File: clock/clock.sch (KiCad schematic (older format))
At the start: 166 parts, among them J1 Conn_02x05_Odd_Even, P1 Conn_WallPlug, T1 120 to 5, U1 74HC596, U10 74HC596, U11 LPC804-TSSOP24, U2 74HC596, U3 74HC596, U4 74HC596, U5 74HC596, U6 74HC596, U7 AP2204R-3.3, U8 74HC596, U9 74HC596

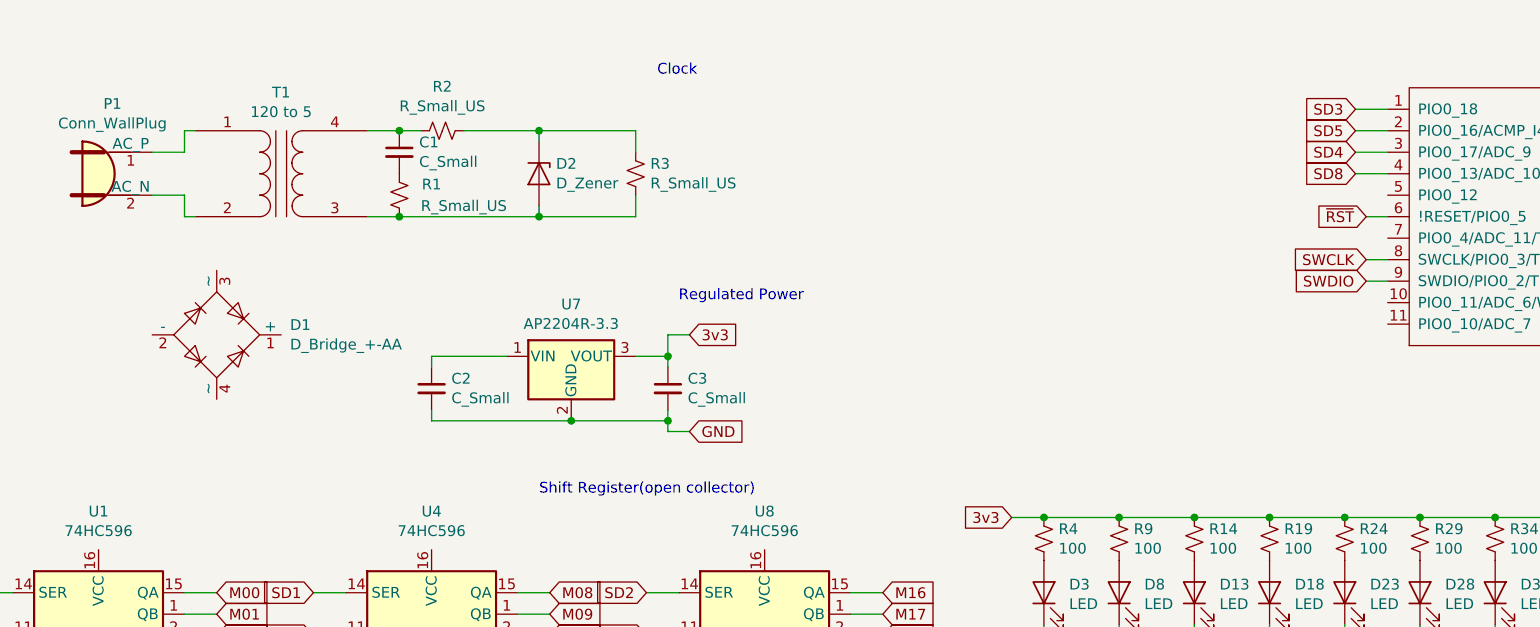
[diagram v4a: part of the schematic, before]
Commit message: Decided on a full wave rectifier. Reevaluated the desired transformer and chose a 120 to 12. Reevaluation due to minimum vin on 3v3 rec is 5v3. Added simulations images from QUCS to the build. QUCS used to design the clock timer edge. I might want to have some means for it to sync milliseconds externally, but that might be the feature creep that kills the project. If there are pins left over, pull them aside as an expansion header.
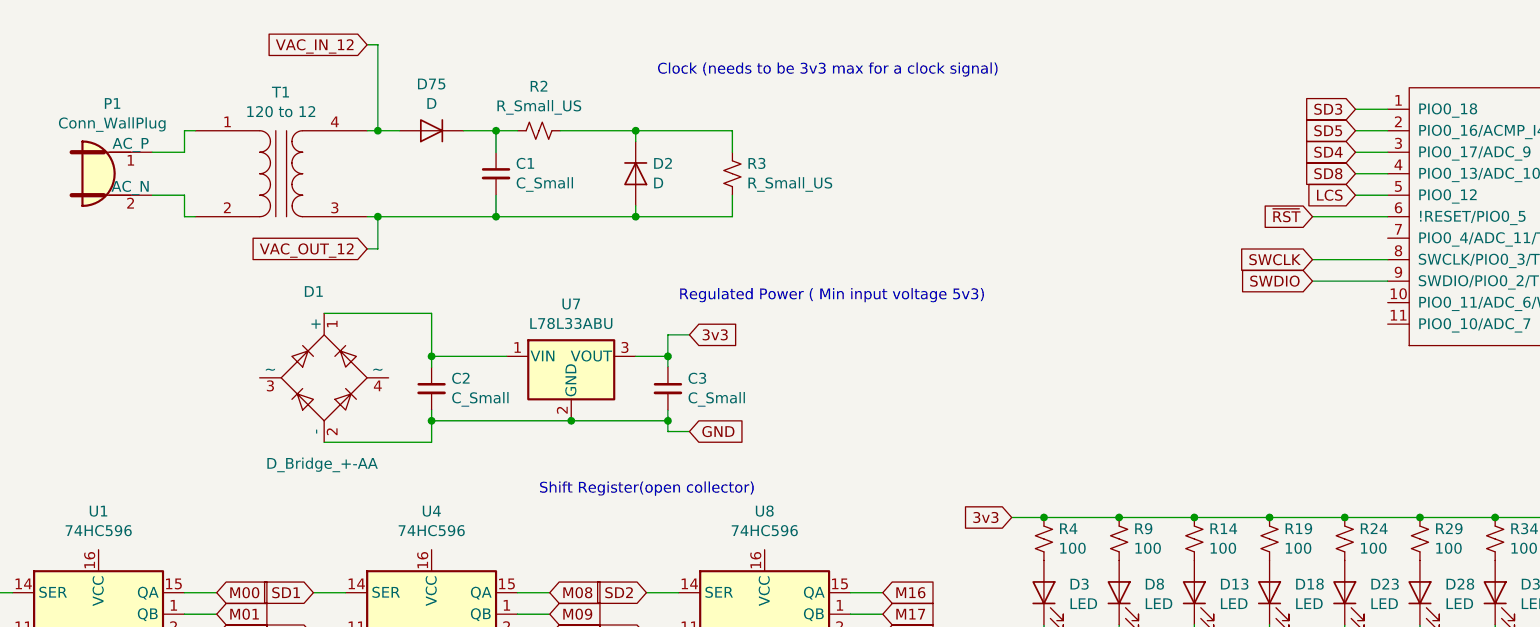
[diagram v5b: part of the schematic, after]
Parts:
- removed D2: D_Zener, symbol Device:D_Zener
- removed R1: R_Small_US, symbol Device:R_Small_US
- added D2, D75: D, symbol Device:D
- T1: value 120 to 5 -> 120 to 12
- U7: value AP2204R-3.3 -> L78L33ABU
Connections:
- net GND: now also D1.2 (-)
- net VAC_OUT_12: now reaches R3.1, T1.3 (SA)
- net VAC_OUT_12: now also C1.2, D2.2 (A)
- net at C1.1, R2.2: now also D75.1 (K); no longer T1.4 (SB)
- net at R2.1, R3.2: now also D2.1 (K)
- net at D1.1 (+): now also C2.1, U7.1 (VIN)
- net LCS: now reaches U11.5 (PIO0_12)
- new net VAC_IN_12: D75.2 (A), T1.4 (SB)
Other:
- note added: "Clock (needs to be 3v3 max for a clock signal)"
- note added: "Regulated Power ( Min input voltage 5v3)"
- note removed: "Clock"
- note removed: "Regulated Power"
- moved on the sheet: C1, D1, R2, R3
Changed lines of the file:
@@
 P 2100 1250
 F 0 "T1" H 2100 1628 50  0000 C CNN
-F 1 "120 to 5" H 2100 1537 50  0000 C CNN
+F 1 "120 to 12" H 2100 1537 50  0000 C CNN
 F 2 "" H 2100 1250 50  0001 C CNN
 F 3 "~" H 2100 1250 50  0001 C CNN
@@
 $EndComp
 $Comp
-L Device:D_Zener D2
-U 1 1 5DF1C116
-P 3300 1250
-F 0 "D2" V 3254 1329 50  0000 L CNN
-F 1 "D_Zener" V 3345 1329 50  0000 L CNN
-F 2 "" H 3300 1250 50  0001 C CNN
-F 3 "~" H 3300 1250 50  0001 C CNN
-	1    3300 1250
-	0    1    1    0
-$EndComp
-$Comp
 L Device:R_Small_US R2
 U 1 1 5DF1C1DC
-P 2850 1050
-F 0 "R2" V 2645 1050 50  0000 C CNN
-F 1 "R_Small_US" V 2736 1050 50  0000 C CNN
-F 2 "" H 2850 1050 50  0001 C CNN
-F 3 "~" H 2850 1050 50  0001 C CNN
-	1    2850 1050
+P 3300 1050
+F 0 "R2" V 3095 1050 50  0000 C CNN
+F 1 "R_Small_US" V 3186 1050 50  0000 C CNN
+F 2 "" H 3300 1050 50  0001 C CNN
+F 3 "~" H 3300 1050 50  0001 C CNN
+	1    3300 1050
 	0    1    1    0
 $EndComp
@@
 L Device:R_Small_US R3
 U 1 1 5DF1C2BA
-P 3750 1250
-F 0 "R3" H 3682 1204 50  0000 R CNN
-F 1 "R_Small_US" H 3682 1295 50  0000 R CNN
-F 2 "" H 3750 1250 50  0001 C CNN
-F 3 "~" H 3750 1250 50  0001 C CNN
-	1    3750 1250
+P 4200 1250
+F 0 "R3" H 4132 1204 50  0000 R CNN
+F 1 "R_Small_US" H 4132 1295 50  0000 R CNN
+F 2 "" H 4200 1250 50  0001 C CNN
+F 3 "~" H 4200 1250 50  0001 C CNN
+	1    4200 1250
 	-1   0    0    1
 $EndComp
@@
 L Device:C_Small C1
 U 1 1 5DF1C4C1
-P 2650 1150
-F 0 "C1" H 2742 1196 50  0000 L CNN
-F 1 "C_Small" H 2742 1105 50  0000 L CNN
-F 2 "" H 2650 1150 50  0001 C CNN
-F 3 "~" H 2650 1150 50  0001 C CNN
-	1    2650 1150
+P 3100 1250
+F 0 "C1" H 3192 1296 50  0000 L CNN
+F 1 "C_Small" H 3192 1205 50  0000 L CNN
+F 2 "" H 3100 1250 50  0001 C CNN
+F 3 "~" H 3100 1250 50  0001 C CNN
+	1    3100 1250
 	1    0    0    -1
 $EndComp
-$Comp
-L Device:R_Small_US R1
-U 1 1 5DF1C5AB
-P 2650 1350
-F 0 "R1" H 2500 1300 50  0000 C CNN
-F 1 "R_Small_US" H 2350 1400 50  0000 C CNN
-F 2 "" H 2650 1350 50  0001 C CNN
-F 3 "~" H 2650 1350 50  0001 C CNN
-	1    2650 1350
-	-1   0    0    1
-$EndComp
 Wire Wire Line
-	2500 1050 2650 1050
+	2950 1050 3100 1050
 Wire Wire Line
-	2650 1050 2750 1050
-Connection ~ 2650 1050
+	3100 1050 3200 1050
 Wire Wire Line
-	2950 1050 3300 1050
+	3400 1050 3750 1050
 Wire Wire Line
-	3300 1050 3300 1100
+	3750 1050 3750 1100
 Wire Wire Line
-	3300 1050 3750 1050
+	3750 1050 4200 1050
 Wire Wire Line
-	3750 1050 3750 1150
-Connection ~ 3300 1050
+	4200 1050 4200 1150
+Connection ~ 3750 1050
 Wire Wire Line
-	2500 1450 2650 1450
+	3750 1450 3750 1400
 Wire Wire Line
-	2650 1450 3300 1450
+	3750 1450 4200 1450
 Wire Wire Line
-	3300 1450 3300 1400
-Connection ~ 2650 1450
-Wire Wire Line
-	3300 1450 3750 1450
-Wire Wire Line
-	3750 1450 3750 1350
-Connection ~ 3300 1450
+	4200 1450 4200 1350
+Connection ~ 3750 1450
 $Comp
 L Connector:Conn_WallPlug P1
@@
 L Device:D_Bridge_+-AA D1
 U 1 1 5DF1D760
-P 1800 2000
-F 0 "D1" H 2141 2046 50  0000 L CNN
-F 1 "D_Bridge_+-AA" H 2141 1955 50  0000 L CNN
-F 2 "" H 1800 2000 50  0001 C CNN
-F 3 "~" H 1800 2000 50  0001 C CNN
-	1    1800 2000
-	1    0    0    -1
+P 2300 2200
+F 0 "D1" V 2700 2200 50  0000 L CNN
+F 1 "D_Bridge_+-AA" V 1900 1950 50  0000 L CNN
+F 2 "" H 2300 2200 50  0001 C CNN
+F 3 "~" H 2300 2200 50  0001 C CNN
+	1    2300 2200
+	0    -1   -1   0
 $EndComp
 $Comp
@@
 P 3450 2100
 F 0 "U7" H 3450 2342 50  0000 C CNN
-F 1 "AP2204R-3.3" H 3450 2251 50  0000 C CNN
+F 1 "L78L33ABU" H 3450 2251 50  0000 C CNN
 F 2 "Package_TO_SOT_SMD:SOT-89-3" H 3450 2325 50  0001 C CNN
 F 3 "https://www.diodes.com/assets/Datasheets/AP2204.pdf" H 3450 2100 50  0001 C CNN
@@
 $EndComp
 Text Notes 3850 800  0    50   ~ 0
-Clock
+Clock (needs to be 3v3 max for a clock signal)
 Text Notes 3950 1850 0    50   ~ 0
-Regulated Power
+Regulated Power ( Min input voltage 5v3)
 Text Notes 3300 2750 0    50   ~ 0
 Shift Register(open collector)
@@
 Wire Wire Line
 	10800 2500 10900 2500
-Text GLabel 7150 1750 0    50   Input ~ 0
+Text GLabel 6900 1750 0    50   Input ~ 0
 SWDIO
-Text GLabel 7150 1650 0    50   Input ~ 0
+Text GLabel 6900 1650 0    50   Input ~ 0
 SWCLK
 Wire Wire Line
-	7150 1650 7250 1650
+	6900 1650 7250 1650
 Wire Wire Line
-	7150 1750 7250 1750
-Text GLabel 7150 1450 0    50   Input ~ 0
+	6900 1750 7250 1750
+Text GLabel 6900 1450 0    50   Input ~ 0
 ~RST
 Wire Wire Line
-	7150 1450 7250 1450
+	6900 1450 7250 1450
 Text GLabel 8350 750  0    50   Input ~ 0
 3v3
@@
 Wire Wire Line
 	1650 7200 1800 7200
+Wire Wire Line
+	2300 1900 2800 1900
+Wire Wire Line
+	2800 1900 2800 2100
+Connection ~ 2800 2100
+Wire Wire Line
+	2300 2500 2800 2500
+Wire Wire Line
+	2800 2500 2800 2400
+Connection ~ 2800 2400
+$Comp
+L Device:D D2
+U 1 1 5E0C20B6
+P 3750 1250
+F 0 "D2" V 3704 1329 50  0000 L CNN
+F 1 "D" V 3795 1329 50  0000 L CNN
+F 2 "" H 3750 1250 50  0001 C CNN
+F 3 "~" H 3750 1250 50  0001 C CNN
+	1    3750 1250
+	0    1    1    0
+$EndComp
+Text GLabel 7100 1350 0    50   Input ~ 0
+LCS
+Wire Wire Line
+	7100 1350 7250 1350
+$Comp
+L Device:D D75
+U 1 1 5E1E6D4D
+P 2800 1050
+F 0 "D75" H 2800 834 50  0000 C CNN
+F 1 "D" H 2800 925 50  0000 C CNN
+F 2 "" H 2800 1050 50  0001 C CNN
+F 3 "~" H 2800 1050 50  0001 C CNN
+	1    2800 1050
+	-1   0    0    1
+$EndComp
+Wire Wire Line
+	2500 1050 2550 1050
+Wire Wire Line
+	2500 1450 2550 1450
+Connection ~ 3100 1050
+Wire Wire Line
+	3100 1050 3100 1150
+Wire Wire Line
+	3100 1350 3100 1450
+Connection ~ 3100 1450
+Wire Wire Line
+	3100 1450 3750 1450
+Text GLabel 2500 650  0    50   Input ~ 0
+VAC_IN_12
+Text GLabel 2500 1600 0    50   Input ~ 0
+VAC_OUT_12
+Wire Wire Line
+	2500 1600 2550 1600
+Wire Wire Line
+	2550 1600 2550 1450
+Connection ~ 2550 1450
+Wire Wire Line
+	2550 1450 3100 1450
+Wire Wire Line
+	2500 650  2550 650
+Wire Wire Line
+	2550 650  2550 1050
+Connection ~ 2550 1050
+Wire Wire Line
+	2550 1050 2650 1050
 $EndSCHEMATC

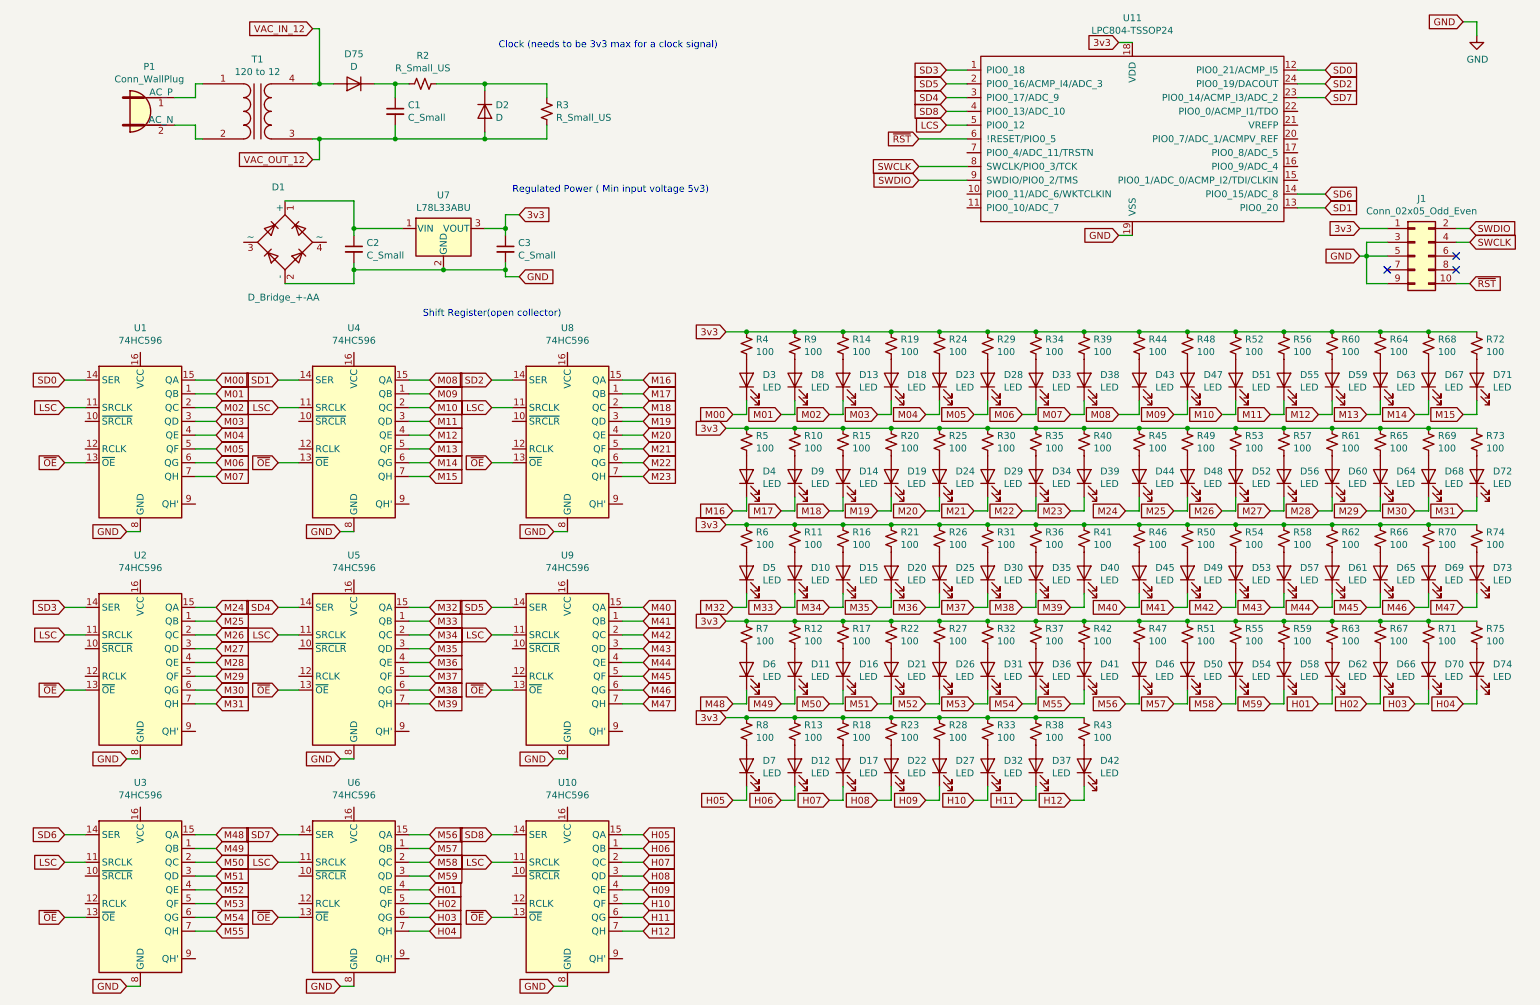
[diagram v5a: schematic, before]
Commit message: Correct QUCS sim to adhere more to reality. Noticed incongruity between 596 foot print and default KiCAD schematic symbol.
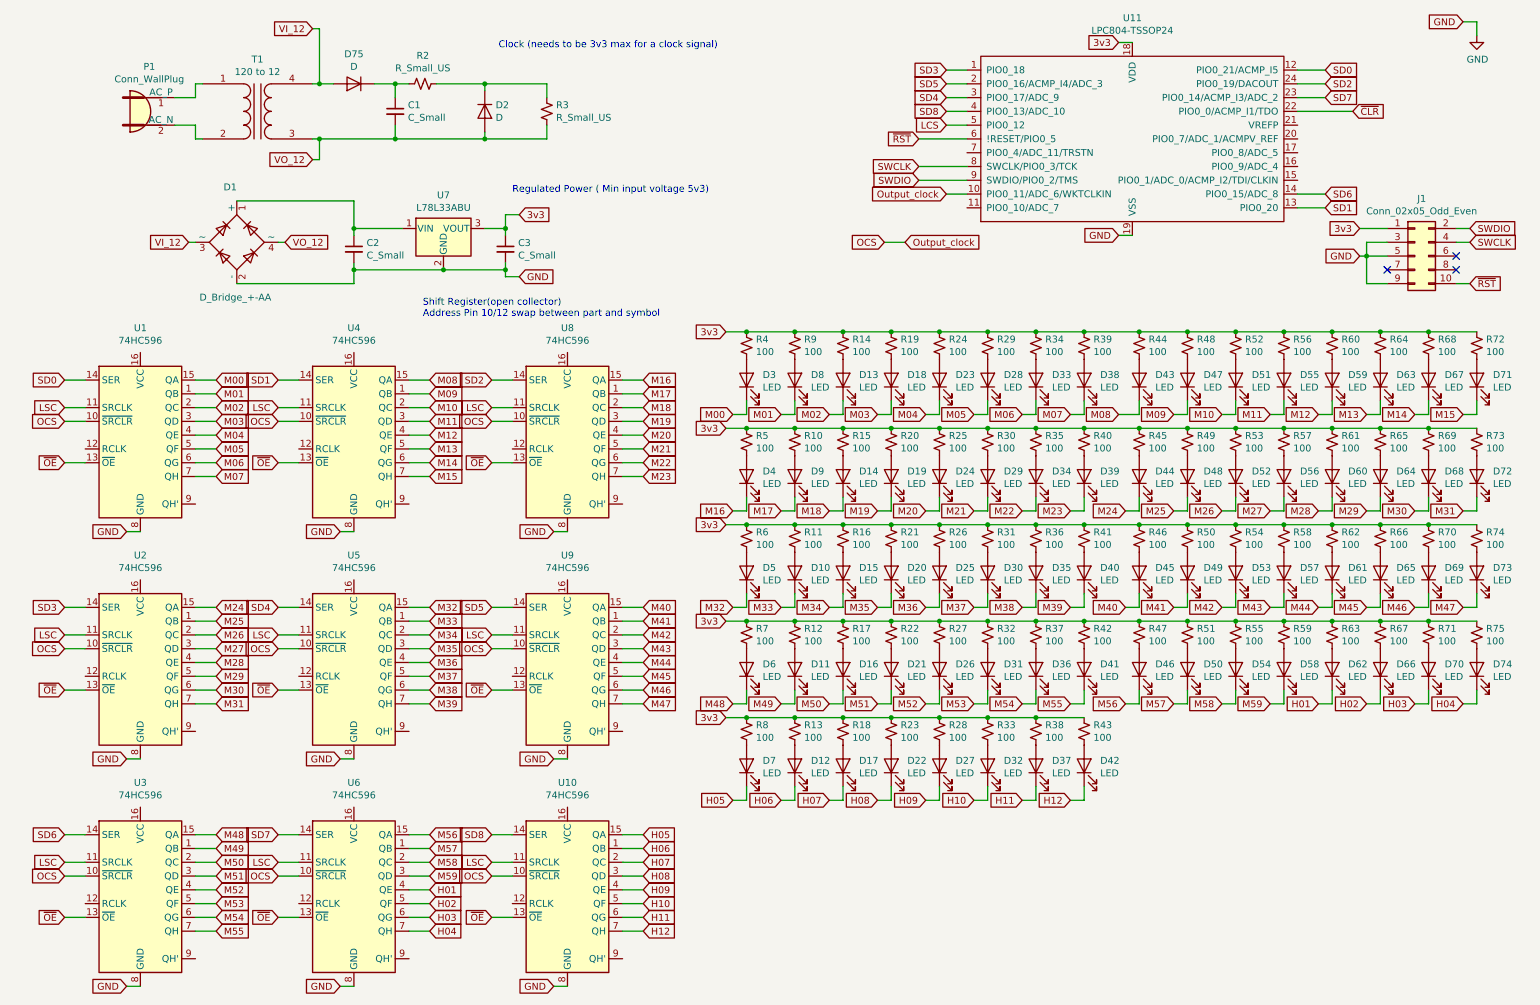
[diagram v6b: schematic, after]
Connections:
- net VAC_IN_12 is gone; now on net VI_12: D75.2 (A), T1.4 (SB)
- net VAC_OUT_12 is gone; now on net VO_12: C1.2, D2.2 (A), R3.1, T1.3 (SA)
- net VI_12: now reaches D1.3 (~~)
- net VO_12: now reaches D1.4 (~~)
- net OCS: now reaches U1.10 (~SRCLR)
- net OCS: now also U10.10 (~SRCLR), U11.10 (PIO0_11/ADC_6/WKTCLKIN), U2.10 (~SRCLR), U3.10 (~SRCLR), U4.10 (~SRCLR), U5.10 (~SRCLR), U6.10 (~SRCLR), U8.10 (~SRCLR), U9.10 (~SRCLR)
- net ~CLR: now reaches U11.22 (PIO0_0/ACMP_I1/TDO)
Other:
- note added: "Shift Register(open collector)\nAddress Pin 10/12 swap between part and symbol"
- note removed: "Shift Register(open collector)"
- moved on the sheet: D1
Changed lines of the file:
@@
 L Device:D_Bridge_+-AA D1
 U 1 1 5DF1D760
-P 2300 2200
-F 0 "D1" V 2700 2200 50  0000 L CNN
-F 1 "D_Bridge_+-AA" V 1900 1950 50  0000 L CNN
-F 2 "" H 2300 2200 50  0001 C CNN
-F 3 "~" H 2300 2200 50  0001 C CNN
-	1    2300 2200
+P 1950 2200
+F 0 "D1" V 2350 2200 50  0000 L CNN
+F 1 "D_Bridge_+-AA" V 1550 1950 50  0000 L CNN
+F 2 "" H 1950 2200 50  0001 C CNN
+F 3 "~" H 1950 2200 50  0001 C CNN
+	1    1950 2200
 	0    -1   -1   0
 $EndComp
@@
 Regulated Power ( Min input voltage 5v3)
 Text Notes 3300 2750 0    50   ~ 0
-Shift Register(open collector)
+Shift Register(open collector)\nAddress Pin 10/12 swap between part and symbol
 $Comp
 L MCU_NXP_LPC804:LPC804-TSSOP24 U11
@@
 	1650 7200 1800 7200
 Wire Wire Line
-	2300 1900 2800 1900
-Wire Wire Line
 	2800 1900 2800 2100
 Connection ~ 2800 2100
 Wire Wire Line
-	2300 2500 2800 2500
-Wire Wire Line
 	2800 2500 2800 2400
 Connection ~ 2800 2400
@@
 	3100 1450 3750 1450
 Text GLabel 2500 650  0    50   Input ~ 0
-VAC_IN_12
+VI_12
 Text GLabel 2500 1600 0    50   Input ~ 0
-VAC_OUT_12
+VO_12
 Wire Wire Line
 	2500 1600 2550 1600
@@
 Wire Wire Line
 	2550 1050 2650 1050
+Text GLabel 2300 2200 2    50   Input ~ 0
+VO_12
+Wire Wire Line
+	2300 2200 2250 2200
+Text GLabel 1600 2200 0    50   Input ~ 0
+VI_12
+Wire Wire Line
+	1600 2200 1650 2200
+Wire Wire Line
+	1950 1900 2800 1900
+Wire Wire Line
+	1950 2500 2800 2500
+Text GLabel 7100 1850 0    50   Input ~ 0
+Output_clock
+Wire Wire Line
+	7100 1850 7250 1850
+Text GLabel 6800 2200 2    50   Input ~ 0
+Output_clock
+Wire Wire Line
+	6800 2200 6650 2200
+Text GLabel 6650 2200 0    50   Input ~ 0
+OCS
+Wire Wire Line
+	850  3500 700  3500
+Text GLabel 700  3500 0    50   Input ~ 0
+OCS
+Wire Wire Line
+	2400 3500 2250 3500
+Text GLabel 2250 3500 0    50   Input ~ 0
+OCS
+Wire Wire Line
+	3950 3500 3800 3500
+Text GLabel 3800 3500 0    50   Input ~ 0
+OCS
+Wire Wire Line
+	3950 5150 3800 5150
+Text GLabel 3800 5150 0    50   Input ~ 0
+OCS
+Wire Wire Line
+	2400 5150 2250 5150
+Text GLabel 2250 5150 0    50   Input ~ 0
+OCS
+Wire Wire Line
+	850  5150 700  5150
+Text GLabel 700  5150 0    50   Input ~ 0
+OCS
+Wire Wire Line
+	850  6800 700  6800
+Text GLabel 700  6800 0    50   Input ~ 0
+OCS
+Wire Wire Line
+	2400 6800 2250 6800
+Text GLabel 2250 6800 0    50   Input ~ 0
+OCS
+Wire Wire Line
+	3950 6800 3800 6800
+Text GLabel 3800 6800 0    50   Input ~ 0
+OCS
+Text GLabel 10050 1250 2    50   Input ~ 0
+~CLR
+Wire Wire Line
+	9650 1250 10050 1250
 $EndSCHEMATC
